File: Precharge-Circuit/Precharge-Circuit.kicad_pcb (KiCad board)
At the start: 2 copper layers, 100 x 100 mm, 112 parts, among them J1 S2P-VH, J2 SM04B-PASS-1-TB, J3 SM02B-PASS-1-TB, J4 S2P-VH, J5 S2P-VH, J6 SM03B-PASS-1-TB, J7 19427-0040, J8 19427-0040, K1 G5Q-1A4_DC12, K2 AZDC6-2AE-12D, K3 G5Q-1A4_DC12, Q1 DMP3098LQ-7, Q10 2N7002K-AU, Q2 2N7002K-AU, Q3 PJA3439-AU_R1_000A1, Q4 2N7002K-AU, Q5 PJA3439-AU_R1_000A1, Q6 2N7002K-AU, Q7 PJA3439-AU_R1_000A1, Q8 2N7002K-AU, Q9 2N7002K-AU, U1 TLP291(GB,SE, U2 TLP291(GB,SE, U3 TL431QDBVR, U4 TL431QDBVR

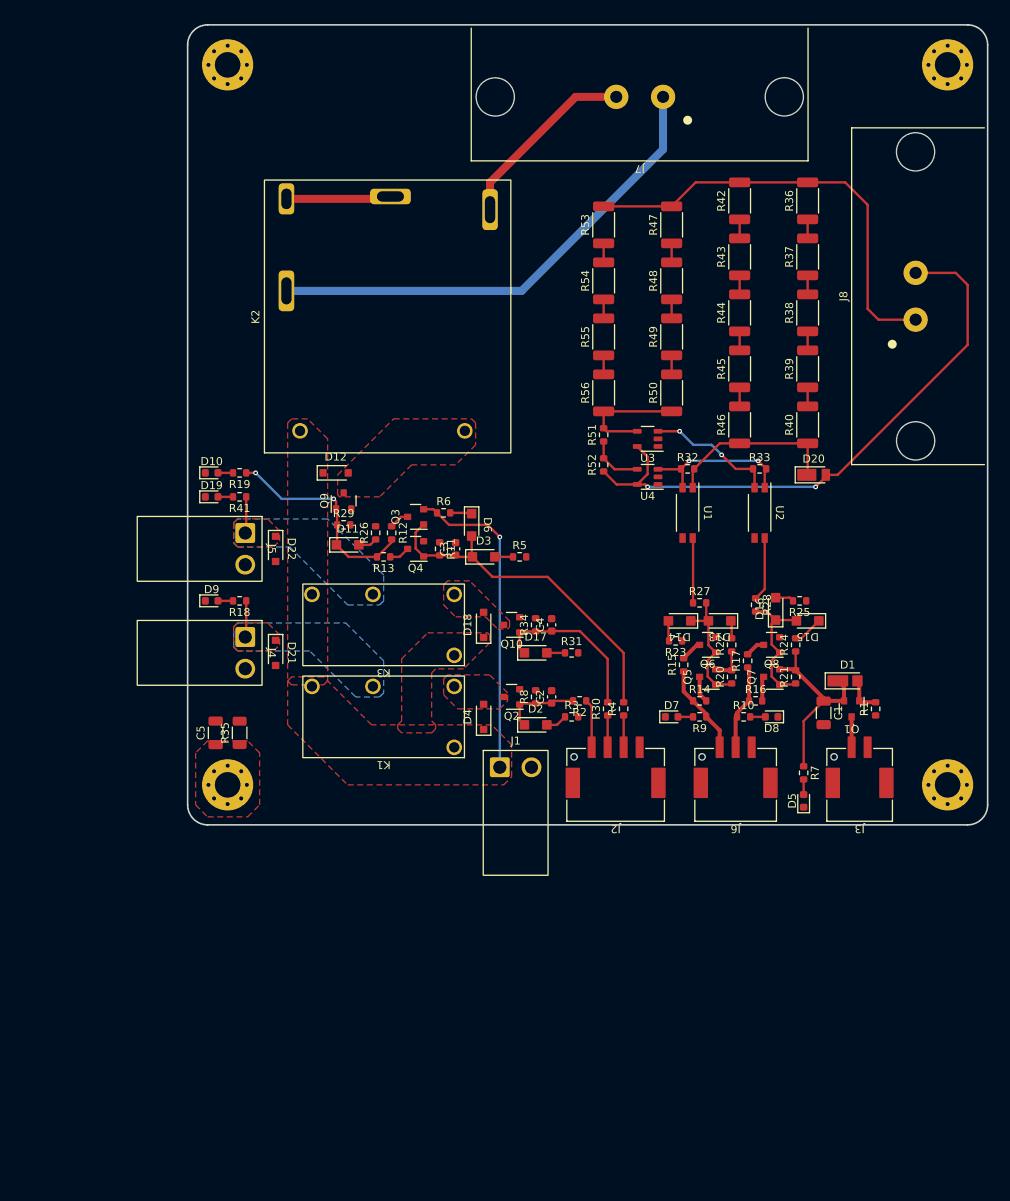
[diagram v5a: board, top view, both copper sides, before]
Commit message: 配線完了、DRC実行エラーなし・警告あり
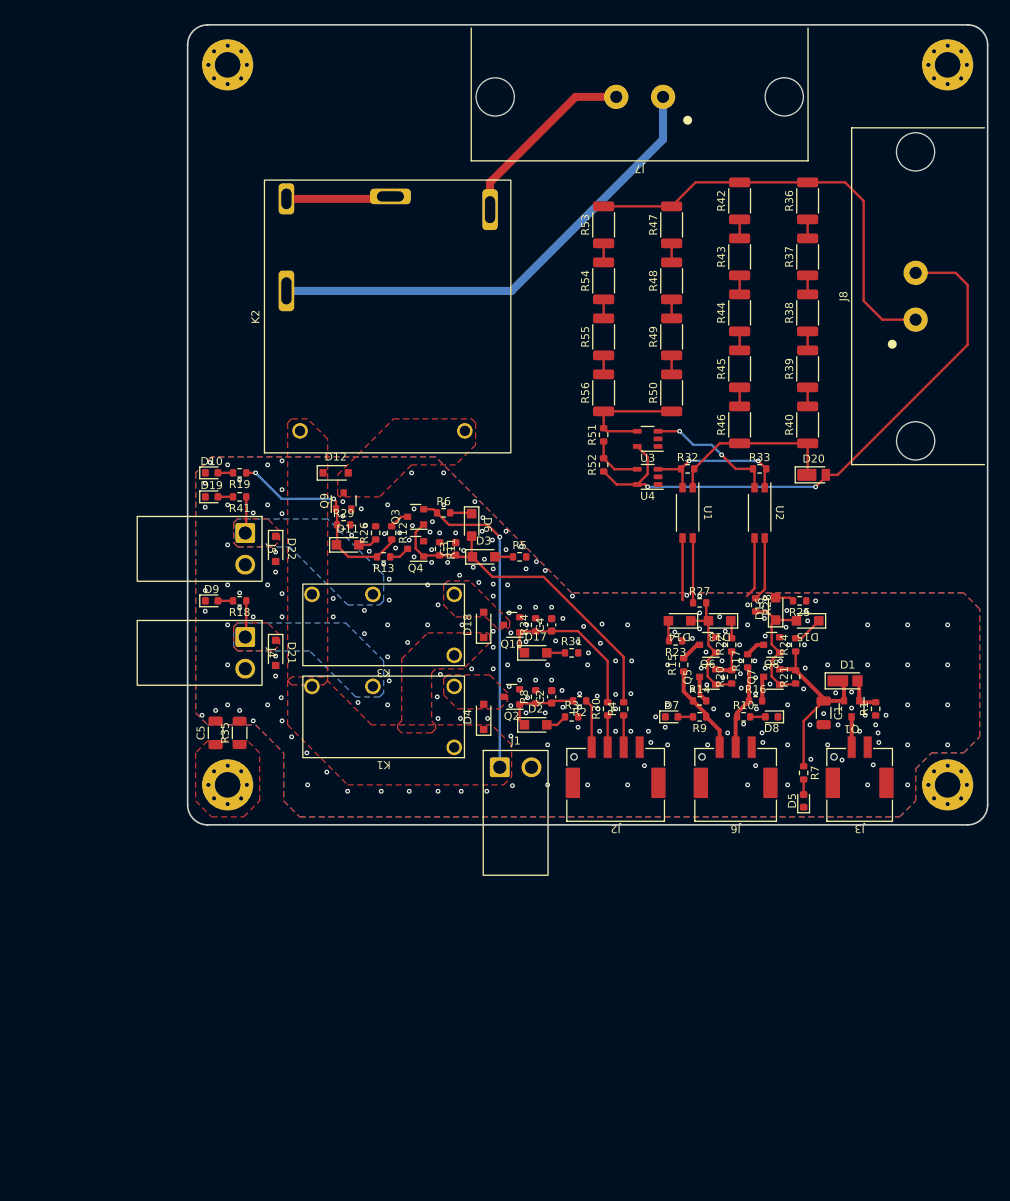
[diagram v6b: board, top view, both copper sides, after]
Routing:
- net GND: track 0.00 -> 15.4 mm, vias 0 -> 253
- net /PCHG_IN: track 61.0 -> 60.2 mm
- added copper zone on B.Cu, net GND
- added copper zone on F.Cu, net GND

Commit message: 完成、配線修正、シルク位置修正、シルク追加
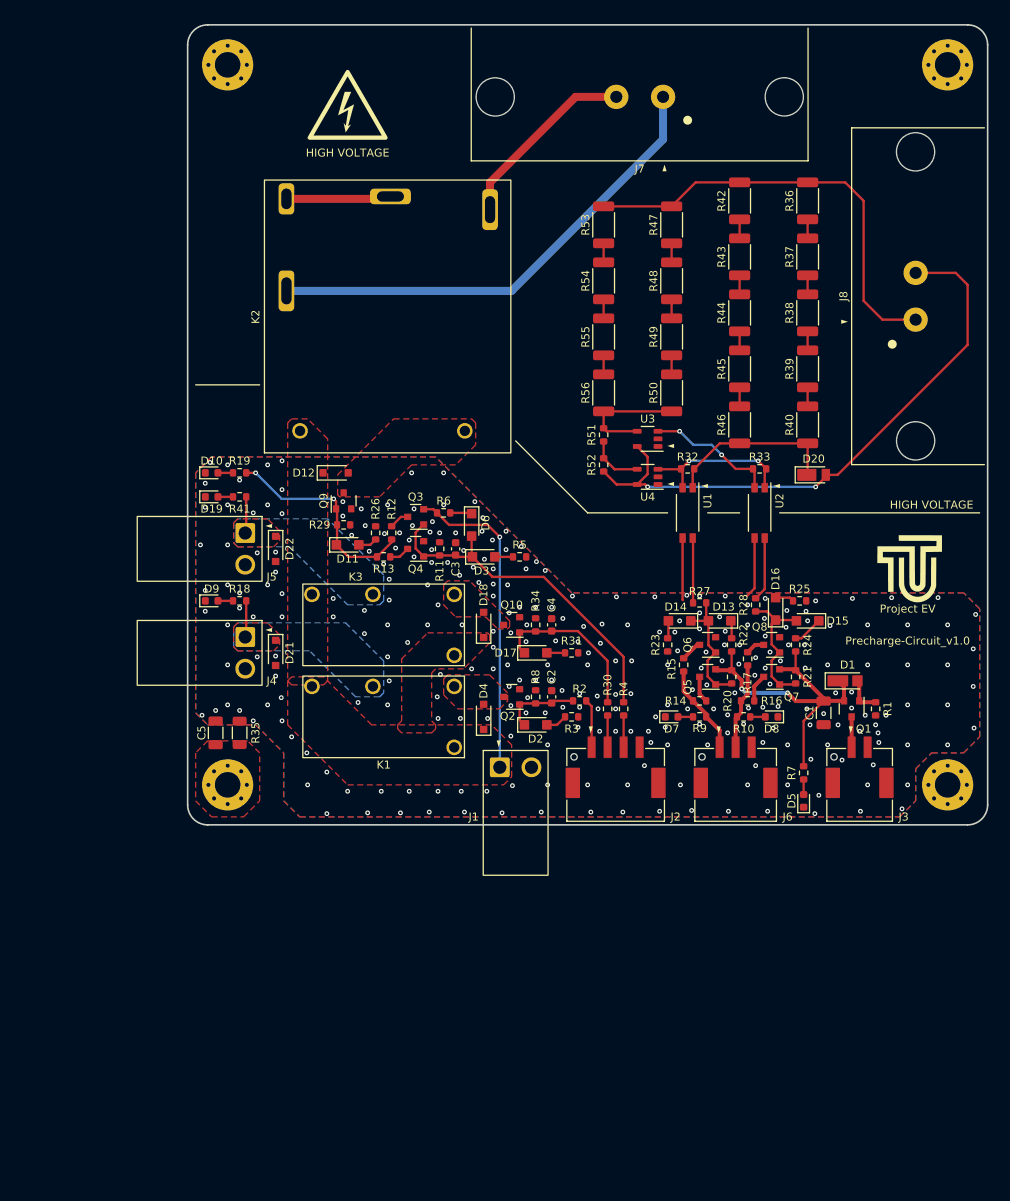
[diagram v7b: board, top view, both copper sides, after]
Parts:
- added G***: ISO_7010_W012, ProjectEV:ISO_7010_W012_10x8.7mm, F.Cu at (120.0, 60.0)
- added G***: Logo_TUT_10x10mm, ProjectEV:Logo_TUT_10x10mm, F.Cu at (190.0, 118.0)
- added G***: ISO_7010_W012, ProjectEV:ISO_7010_W012_10x8.7mm, B.Cu at (170.0, 100.0)
- added REF**: Identifier_1pin, ProjectEV:Identifier_1pin, F.Cu at (109.8, 112.8)
- added REF**: Identifier_1pin, ProjectEV:Identifier_1pin, F.Cu at (109.8, 125.8)
- added REF**: Identifier_1pin, ProjectEV:Identifier_1pin, F.Cu at (164.2, 107.8)
- added REF**: Identifier_1pin, ProjectEV:Identifier_1pin, F.Cu at (150.5, 138.5)
- added REF**: Identifier_1pin, ProjectEV:Identifier_1pin, F.Cu at (182.5, 87.0)
- added REF**: Identifier_1pin, ProjectEV:Identifier_1pin, F.Cu at (160.0, 107.5)
- added REF**: Identifier_1pin, ProjectEV:Identifier_1pin, F.Cu at (166.5, 138.5)
- added REF**: Identifier_1pin, ProjectEV:Identifier_1pin, F.Cu at (183.0, 138.5)
- added REF**: Identifier_1pin, ProjectEV:Identifier_1pin, F.Cu at (159.5, 67.5)
- added REF**: Identifier_1pin, ProjectEV:Identifier_1pin, F.Cu at (173.2, 107.8)
- added REF**: Identifier_1pin, ProjectEV:Identifier_1pin, F.Cu at (160.0, 102.8)
- added REF**: Identifier_1pin, ProjectEV:Identifier_1pin, F.Cu at (139.0, 140.2)
- moved R23 1.12 mm to (160.0, 127.5), turned to 90 degrees
- moved R16 1.00 mm to (170.0, 134.5)
- moved R17 0.25 mm to (170.0, 129.2)
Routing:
- net +12V: track 28.7 -> 42.4 mm, vias 0 -> 2
- net GND: vias 253 -> 287
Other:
- board text added: "HIGH VOLTAGE"
- board text added: "Precharge-Circuit_v1.0"
- board text added: "Project EV"
